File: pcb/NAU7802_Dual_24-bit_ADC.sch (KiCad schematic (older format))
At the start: 22 parts, among them J1 CELL_A, J2 CELL_B, J3 STEMMA_QT, J4 STEMMA_QT, M1 Feather_M4_Express, U1 NAU7802_24bit_ADC

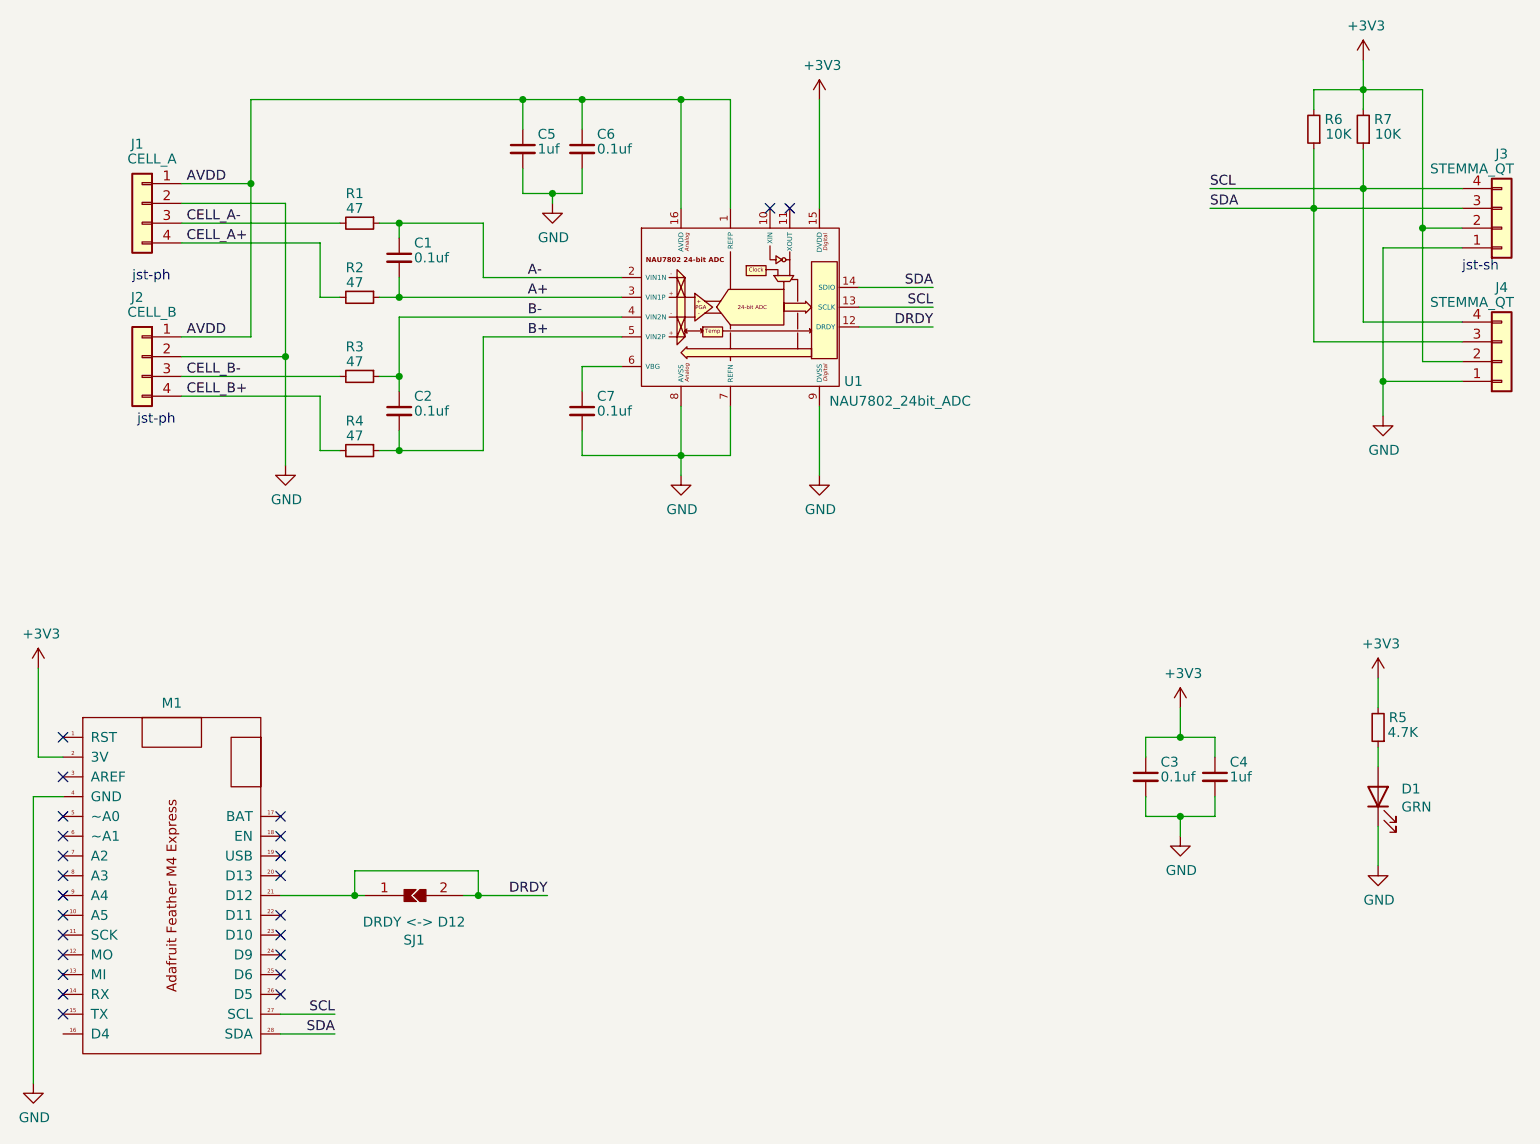
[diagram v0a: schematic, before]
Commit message: update for 2-channel operation
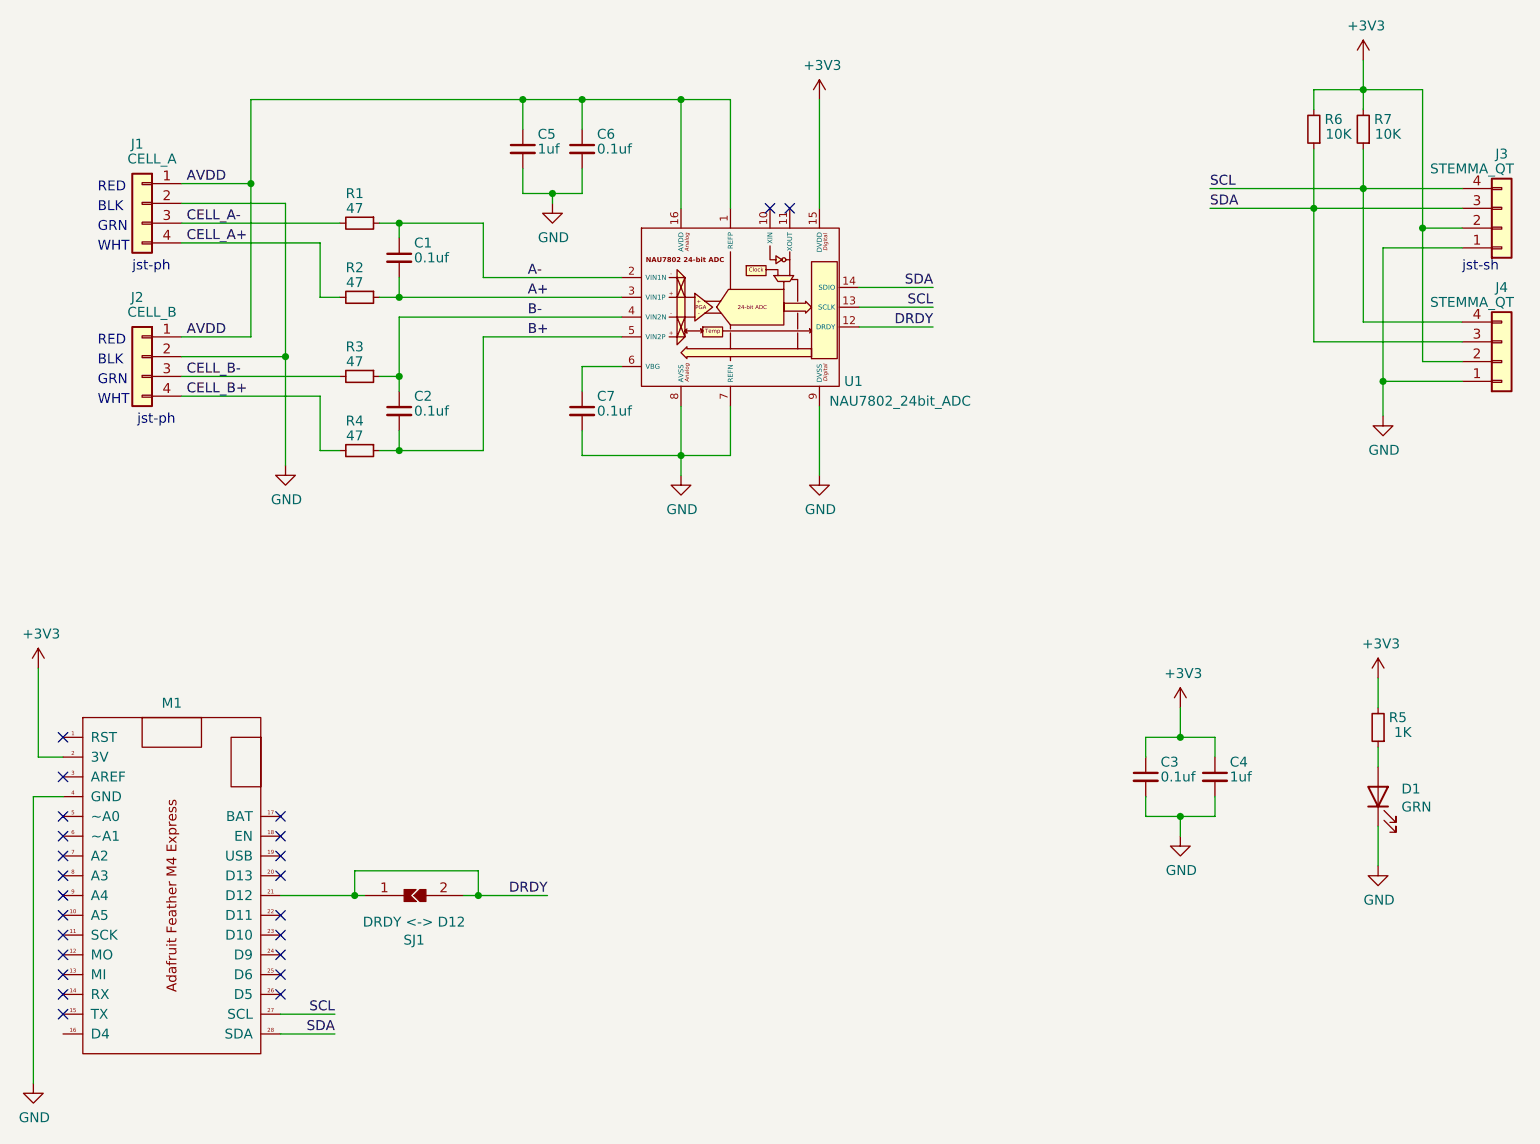
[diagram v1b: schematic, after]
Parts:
- R5: value 4.7K -> 1K
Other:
- note added: "BLK"
- note added: "GRN"
- note added: "RED"
- note added: "WHT"
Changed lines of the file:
@@
 Sheet 1 1
 Title "NAU7802_DUAL_24-BIT_ADC_WING"
-Date "2020-10-21"
-Rev "v00"
+Date "2020-11-26"
+Rev "v01"
 Comp "Cedar Grove Studios"
 Comment1 ""
@@
 	1    0    0    1
 $EndComp
-$Comp
-L Connector_Generic:Conn_01x04 J1
-U 1 1 5F8EBC17
-P 2925 2825
-F 0 "J1" H 2950 3125 50  0000 C CNN
-F 1 "CELL_A" H 2875 3050 50  0000 C CNN
-F 2 "Connector_JST:JST_PH_S4B-PH-SM4-TB_1x04-1MP_P2.00mm_Horizontal" H 2925 2825 50  0001 C CNN
-F 3 "~" H 2925 2825 50  0001 C CNN
-	1    2925 2825
-	-1   0    0    -1
-$EndComp
-$Comp
-L Connector_Generic:Conn_01x04 J2
-U 1 1 5F8EC4A7
-P 2925 3600
-F 0 "J2" H 2950 3900 50  0000 C CNN
-F 1 "CELL_B" H 2875 3825 50  0000 C CNN
-F 2 "Connector_JST:JST_PH_S4B-PH-SM4-TB_1x04-1MP_P2.00mm_Horizontal" H 2925 3600 50  0001 C CNN
-F 3 "~" H 2925 3600 50  0001 C CNN
-	1    2925 3600
-	-1   0    0    -1
-$EndComp
 Wire Wire Line
 	3825 3025 3825 3300
@@
 Text Notes 9600 3175 0    50   ~ 0
 jst-sh
-Text Notes 2875 3225 0    50   ~ 0
+Text Notes 2875 3175 0    50   ~ 0
 jst-ph
 $Comp
@@
 P 9175 5475
 F 0 "R5" H 9075 5425 50  0000 C CNN
-F 1 "4.7K" H 9050 5500 50  0000 C CNN
+F 1 "1K" H 9050 5500 50  0000 C CNN
 F 2 "Resistor_SMD:R_0805_2012Metric" H 9175 5475 50  0001 C CNN
 F 3 "~" H 9175 5475 50  0001 C CNN
@@
 Text Label 4875 3500 0    50   ~ 0
 B+
+Text Notes 2700 2775 0    50   ~ 0
+RED
+Text Notes 2700 2975 0    50   ~ 0
+GRN
+Text Notes 2700 2875 0    50   ~ 0
+BLK
+Text Notes 2700 3075 0    50   ~ 0
+WHT
+Text Notes 2700 3550 0    50   ~ 0
+RED
+Text Notes 2700 3750 0    50   ~ 0
+GRN
+Text Notes 2700 3650 0    50   ~ 0
+BLK
+Text Notes 2700 3850 0    50   ~ 0
+WHT
+$Comp
+L Connector_Generic:Conn_01x04 J1
+U 1 1 5F8EBC17
+P 2925 2825
+F 0 "J1" H 2950 3125 50  0000 C CNN
+F 1 "CELL_A" H 2875 3050 50  0000 C CNN
+F 2 "Connector_JST:JST_PH_S4B-PH-SM4-TB_1x04-1MP_P2.00mm_Horizontal" H 2925 2825 50  0001 C CNN
+F 3 "~" H 2925 2825 50  0001 C CNN
+	1    2925 2825
+	-1   0    0    -1
+$EndComp
+$Comp
+L Connector_Generic:Conn_01x04 J2
+U 1 1 5F8EC4A7
+P 2925 3600
+F 0 "J2" H 2950 3900 50  0000 C CNN
+F 1 "CELL_B" H 2875 3825 50  0000 C CNN
+F 2 "Connector_JST:JST_PH_S4B-PH-SM4-TB_1x04-1MP_P2.00mm_Horizontal" H 2925 3600 50  0001 C CNN
+F 3 "~" H 2925 3600 50  0001 C CNN
+	1    2925 3600
+	-1   0    0    -1
+$EndComp
 $EndSCHEMATC

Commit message: update PCB silk design
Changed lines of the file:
@@
 Text Notes 2700 2775 0    50   ~ 0
 RED
-Text Notes 2700 2975 0    50   ~ 0
+Text Notes 2700 3075 0    50   ~ 0
 GRN
 Text Notes 2700 2875 0    50   ~ 0
 BLK
-Text Notes 2700 3075 0    50   ~ 0
+Text Notes 2700 2975 0    50   ~ 0
 WHT
 Text Notes 2700 3550 0    50   ~ 0
 RED
-Text Notes 2700 3750 0    50   ~ 0
+Text Notes 2700 3850 0    50   ~ 0
 GRN
 Text Notes 2700 3650 0    50   ~ 0
 BLK
-Text Notes 2700 3850 0    50   ~ 0
+Text Notes 2700 3750 0    50   ~ 0
 WHT
 $Comp

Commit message: update PCB design
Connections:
- net AVDD: now also J1.3 (Pin_3), J2.3 (Pin_3); no longer J1.1 (Pin_1), J2.1 (Pin_1)
- net CELL_A+: now also J1.1 (Pin_1); no longer J1.4 (Pin_4)
- net CELL_A-: now also J1.2 (Pin_2); no longer J1.3 (Pin_3)
- net CELL_B+: now also J2.1 (Pin_1); no longer J2.4 (Pin_4)
- net CELL_B-: now also J2.2 (Pin_2); no longer J2.3 (Pin_3)
- net GND: now also J1.4 (Pin_4), J2.4 (Pin_4); no longer J1.2 (Pin_2), J2.2 (Pin_2)
- no-connect marks 24 -> 25
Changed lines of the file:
@@
 Sheet 1 1
 Title "NAU7802_DUAL_24-BIT_ADC_WING"
-Date "2020-11-26"
-Rev "v01"
+Date "2020-11-28"
+Rev "v02"
 Comp "Cedar Grove Studios"
 Comment1 ""
@@
 Wire Wire Line
 	3475 3500 3475 2725
-Wire Wire Line
-	3475 2300 4850 2300
 Connection ~ 4850 2300
-Connection ~ 3475 2725
-Wire Wire Line
-	3475 2725 3475 2300
 Wire Wire Line
 	3650 2825 3650 3600
@@
 L power:GND #PWR01
 U 1 1 5F911CA6
-P 3650 4150
-F 0 "#PWR01" H 3650 3900 50  0001 C CNN
-F 1 "GND" H 3655 3977 50  0000 C CNN
-F 2 "" H 3650 4150 50  0001 C CNN
-F 3 "" H 3650 4150 50  0001 C CNN
-	1    3650 4150
-	1    0    0    -1
-$EndComp
-Connection ~ 3650 3600
-Wire Wire Line
-	3650 3600 3650 4150
+P 3475 4150
+F 0 "#PWR01" H 3475 3900 50  0001 C CNN
+F 1 "GND" H 3480 3977 50  0000 C CNN
+F 2 "" H 3475 4150 50  0001 C CNN
+F 3 "" H 3475 4150 50  0001 C CNN
+	1    3475 4150
+	1    0    0    -1
+$EndComp
 Text Notes 9600 3175 0    50   ~ 0
 jst-sh
-Text Notes 2875 3175 0    50   ~ 0
+Text Notes 2875 3150 0    50   ~ 0
 jst-ph
 $Comp
@@
 Wire Wire Line
 	8175 5925 8350 5925
-Text Notes 2900 3950 0    50   ~ 0
+Text Notes 2875 3925 0    50   ~ 0
 jst-ph
 $Comp
@@
 	1    0    0    -1
 $EndComp
-Text Label 3150 2725 0    50   ~ 0
+Text Label 3150 2825 0    50   ~ 0
 AVDD
 Text Label 3150 2925 0    50   ~ 0
@@
 	3125 3500 3475 3500
 Wire Wire Line
-	3125 3600 3650 3600
-Wire Wire Line
 	3125 3700 3925 3700
 Wire Wire Line
 	3125 3800 3825 3800
-Text Label 3150 3500 0    50   ~ 0
+Text Label 3150 3600 0    50   ~ 0
 AVDD
 Text Label 4875 3200 0    50   ~ 0
@@
 Text Label 4875 3500 0    50   ~ 0
 B+
-Text Notes 2700 2775 0    50   ~ 0
+Text Notes 2675 2850 0    50   ~ 0
 RED
-Text Notes 2700 3075 0    50   ~ 0
+Text Notes 2675 3050 0    50   ~ 0
 GRN
-Text Notes 2700 2875 0    50   ~ 0
+Text Notes 2675 2750 0    50   ~ 0
 BLK
-Text Notes 2700 2975 0    50   ~ 0
+Text Notes 2675 2950 0    50   ~ 0
 WHT
-Text Notes 2700 3550 0    50   ~ 0
+Text Notes 2675 3625 0    50   ~ 0
 RED
-Text Notes 2700 3850 0    50   ~ 0
+Text Notes 2675 3825 0    50   ~ 0
 GRN
-Text Notes 2700 3650 0    50   ~ 0
+Text Notes 2675 3525 0    50   ~ 0
 BLK
-Text Notes 2700 3750 0    50   ~ 0
+Text Notes 2675 3725 0    50   ~ 0
 WHT
+$Comp
+L Connector_Generic:Conn_01x04 J2
+U 1 1 5F8EC4A7
+P 2925 3700
+F 0 "J2" H 2925 3325 50  0000 C CNN
+F 1 "CELL_B" H 2850 3400 50  0000 C CNN
+F 2 "Connector_JST:JST_PH_S4B-PH-SM4-TB_1x04-1MP_P2.00mm_Horizontal" H 2925 3700 50  0001 C CNN
+F 3 "~" H 2925 3700 50  0001 C CNN
+	1    2925 3700
+	-1   0    0    1
+$EndComp
 $Comp
 L Connector_Generic:Conn_01x04 J1
 U 1 1 5F8EBC17
-P 2925 2825
-F 0 "J1" H 2950 3125 50  0000 C CNN
-F 1 "CELL_A" H 2875 3050 50  0000 C CNN
-F 2 "Connector_JST:JST_PH_S4B-PH-SM4-TB_1x04-1MP_P2.00mm_Horizontal" H 2925 2825 50  0001 C CNN
-F 3 "~" H 2925 2825 50  0001 C CNN
-	1    2925 2825
-	-1   0    0    -1
-$EndComp
-$Comp
-L Connector_Generic:Conn_01x04 J2
-U 1 1 5F8EC4A7
-P 2925 3600
-F 0 "J2" H 2950 3900 50  0000 C CNN
-F 1 "CELL_B" H 2875 3825 50  0000 C CNN
-F 2 "Connector_JST:JST_PH_S4B-PH-SM4-TB_1x04-1MP_P2.00mm_Horizontal" H 2925 3600 50  0001 C CNN
-F 3 "~" H 2925 3600 50  0001 C CNN
-	1    2925 3600
-	-1   0    0    -1
-$EndComp
+P 2925 2925
+F 0 "J1" H 2925 2550 50  0000 C CNN
+F 1 "CELL_A" H 2850 2625 50  0000 C CNN
+F 2 "Connector_JST:JST_PH_S4B-PH-SM4-TB_1x04-1MP_P2.00mm_Horizontal" H 2925 2925 50  0001 C CNN
+F 3 "~" H 2925 2925 50  0001 C CNN
+	1    2925 2925
+	-1   0    0    1
+$EndComp
+Wire Wire Line
+	3650 2300 4850 2300
+Wire Wire Line
+	3650 2300 3650 2825
+Connection ~ 3650 2825
+Wire Wire Line
+	3125 3600 3650 3600
+Wire Wire Line
+	3475 3500 3475 4150
+Connection ~ 3475 3500
+Text Label 3650 2300 0    50   ~ 0
+AVDD
+NoConn ~ 2525 7025
 $EndSCHEMATC
